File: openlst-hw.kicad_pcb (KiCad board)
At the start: 4 copper layers, 95.9 x 90.2 mm, 170 parts, among them J2 CC Prog/Debug, J3 UART0, J4 UART1, J5 Control Outputs, J6 ANT, J7 PC104-1, J8 PC104-2, U1 LM1117-3.3, U2 CC1110, U3 RFFM6406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

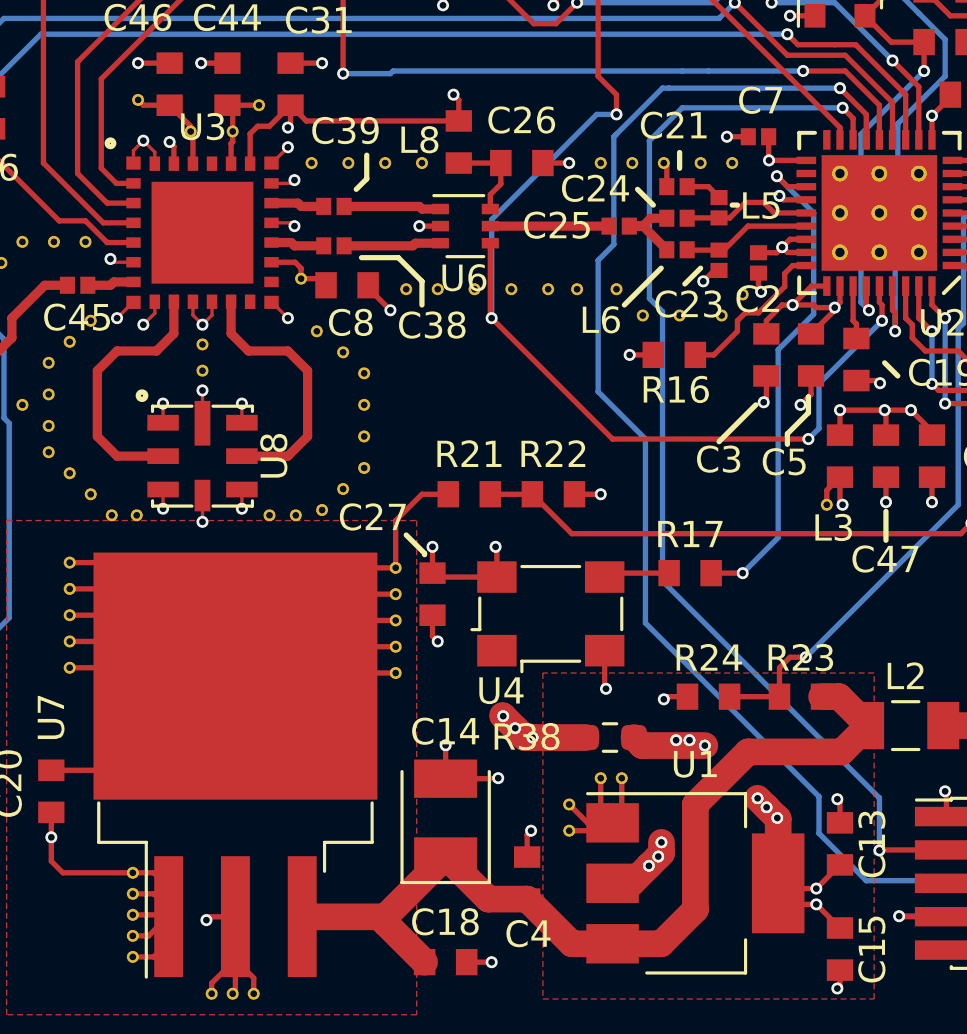
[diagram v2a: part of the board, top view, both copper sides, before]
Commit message: CAM: updated layout to fix some issues with ground plane arrangement
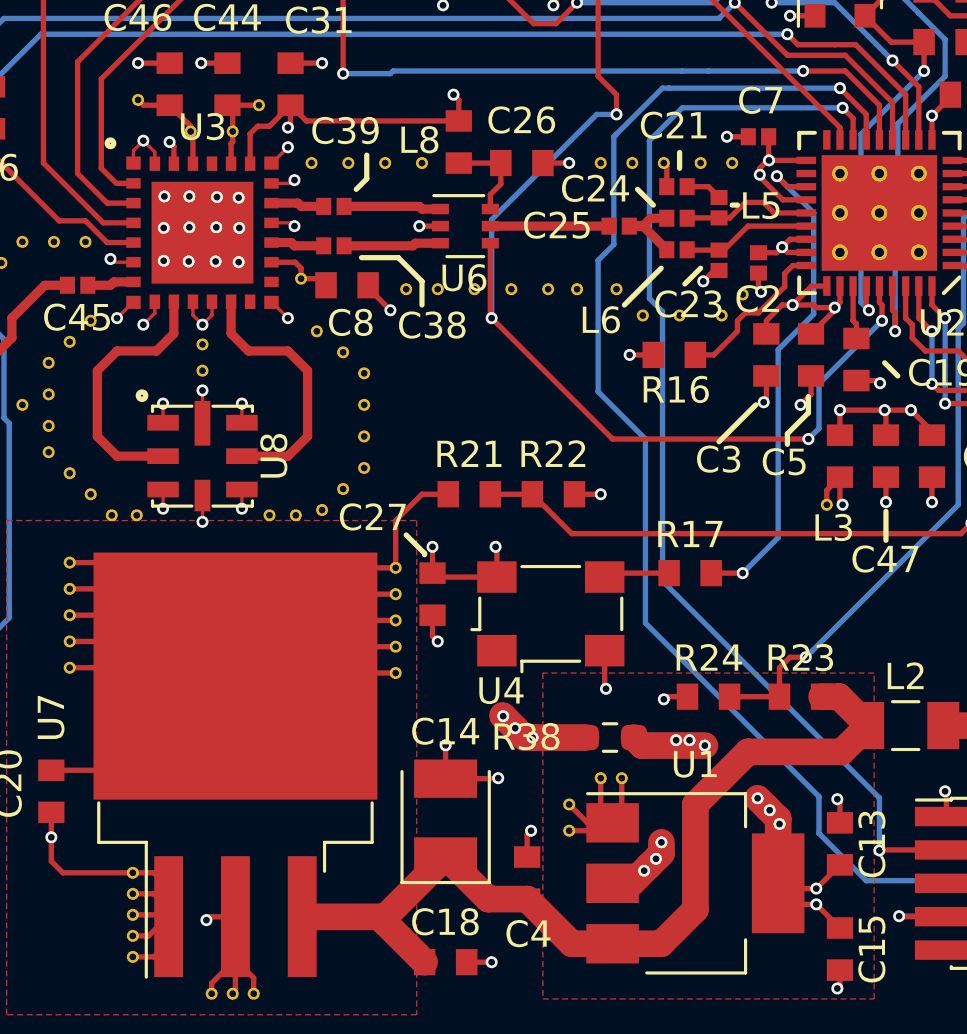
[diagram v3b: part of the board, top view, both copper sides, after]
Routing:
- net /3V3_FILT: track 24.4 -> 26.2 mm
- net GND: vias 59 -> 71
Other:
- board text removed: "This work is licensed under a Creative Commons Attribution-ShareAlike 4.0 International License (CC-BY-SA 4.0)."
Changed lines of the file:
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@@
     (effects (font (size 1 1) (thickness 0.15)) (justify mirror))
-  )
-  (gr_text "This work is licensed under a\nCreative Commons Attribution-ShareAlike 4.0\nInternational License (CC-BY-SA 4.0)." (at 69.5738 164.5054 180) (layer "B.SilkS")
-    (effects (font (size 1 1) (thickness 0.15)) (justify left mirror))
   )
   (gr_text "~{RX}" (at 87.6738 125.1054 180) (layer "F.SilkS")
@@
   (segment (start 104.5738 140.5054) (end 103.8738 140.5054) (width 0.2032) (layer "F.Cu") (net 1))
   (segment (start 102.0738 135.3054) (end 102.7738 134.6054) (width 0.2032) (layer "F.Cu") (net 1))
-  (segment (start 96.4238 138.5054) (end 96.2738 138.3554) (width 0.2032) (layer "F.Cu") (net 1))
   (segment (start 100.3238 146.5554) (end 100.2738 146.5054) (width 0.2032) (layer "F.Cu") (net 1))
   (segment (start 101.2738 146.5054) (end 102.0738 147.3054) (width 0.2032) (layer "F.Cu") (net 1))
   (segment (start 100.2738 146.5054) (end 98.5738 146.5054) (width 0.2032) (layer "F.Cu") (net 1))
   (segment (start 100.3238 147.4554) (end 100.3238 146.5554) (width 0.2032) (layer "F.Cu") (net 1))
+  (segment (start 95.525 137.55) (end 95.525 137.633443) (width 0.2032) (layer "F.Cu") (net 1))
   (segment (start 98.3738 142.6054) (end 98.3738 142.7054) (width 0.2032) (layer "F.Cu") (net 1))
   (segment (start 102.7738 134.5054) (end 102.7738 134.6054) (width 0.2032) (layer "F.Cu") (net 1))
@@
   (segment (start 104.8238 140.7554) (end 104.8238 141.4554) (width 0.2032) (layer "F.Cu") (net 1))
   (segment (start 98.5738 141.7854) (end 98.5738 142.4054) (width 0.2032) (layer "F.Cu") (net 1))
+  (segment (start 95.525 137.55) (end 95.525 137.3) (width 0.2032) (layer "F.Cu") (net 1))
   (segment (start 97.4938 141.7854) (end 98.0738 141.7854) (width 0.2032) (layer "F.Cu") (net 1))
+  (segment (start 96.396957 138.5054) (end 97.2938 138.5054) (width 0.2032) (layer "F.Cu") (net 1))
   (segment (start 95.8613 136.1054) (end 95.8613 136.9929) (width 0.2032) (layer "F.Cu") (net 1))
   (segment (start 98.3738 142.6054) (end 97.6738 142.6054) (width 0.2032) (layer "F.Cu") (net 1))
@@
   (segment (start 95.4738 140.5179) (end 96.1613 140.5179) (width 0.2032) (layer "F.Cu") (net 1))
   (segment (start 95.8738 137.0054) (end 97.2938 137.0054) (width 0.2032) (layer "F.Cu") (net 1))
+  (segment (start 95.525 137.3) (end 95.8196 137.0054) (width 0.2032) (layer "F.Cu") (net 1))
+  (segment (start 95.525 137.633443) (end 96.396957 138.5054) (width 0.2032) (layer "F.Cu") (net 1))
   (segment (start 102.0738 136.2254) (end 102.0738 135.3054) (width 0.2032) (layer "F.Cu") (net 1))
+  (segment (start 95.8196 137.0054) (end 95.8738 137.0054) (width 0.2032) (layer "F.Cu") (net 1))
   (segment (start 102.0738 147.4554) (end 102.0738 147.3054) (width 0.2032) (layer "F.Cu") (net 1))
   (segment (start 102.8538 140.5054) (end 103.8738 140.5054) (width 0.2032) (layer "F.Cu") (net 1))
   (segment (start 95.7738 143.6054) (end 95.7738 143.1054) (width 0.2032) (layer "F.Cu") (net 1))
   (segment (start 98.5738 147.4554) (end 98.5738 146.5054) (width 0.2032) (layer "F.Cu") (net 1))
-  (segment (start 97.2938 138.5054) (end 96.4238 138.5054) (width 0.2032) (layer "F.Cu") (net 1))
   (via (at 102.0738 135.3054) (size 0.4572) (drill 0.254) (layers "F.Cu" "B.Cu") (net 1))
+  (via (at 95.525 137.55) (size 0.4572) (drill 0.254) (layers "F.Cu" "B.Cu") (net 1))
   (via (at 96.7738 142.5054) (size 0.4572) (drill 0.254) (layers "F.Cu" "B.Cu") (net 1))
   (via (at 103.8738 140.5054) (size 0.4572) (drill 0.254) (layers "F.Cu" "B.Cu") (net 1))
@@
   (via (at 100.2738 146.5054) (size 0.4572) (drill 0.254) (layers "F.Cu" "B.Cu") (net 1))
   (via (at 101.2738 146.5054) (size 0.4572) (drill 0.254) (layers "F.Cu" "B.Cu") (net 1))
-  (via (at 96.2738 138.3554) (size 0.4572) (drill 0.254) (layers "F.Cu" "B.Cu") (net 1))
   (via (at 98.5738 146.5054) (size 0.4572) (drill 0.254) (layers "F.Cu" "B.Cu") (net 1))
   (segment (start 76.9738 142.4054) (end 77.5738 143.0054) (width 0.127) (layer "F.Cu") (net 2))
@@
   (via (at 102.5738 161.0054) (size 0.4572) (drill 0.254) (layers "F.Cu" "B.Cu") (net 2))
   (via (at 83.5738 159.2554) (size 0.4572) (drill 0.254) (layers "F.Cu" "B.Cu") (net 2))
+  (via (at 75.7 140.875) (size 0.4572) (drill 0.254) (layers "F.Cu" "B.Cu") (net 2))
   (via (at 77.5738 143.0054) (size 0.4572) (drill 0.254) (layers "F.Cu" "B.Cu") (net 2))
   (via (at 100.0988 145.4804) (size 0.4572) (drill 0.254) (layers "F.Cu" "B.Cu") (net 2))
@@
   (via (at 77.5738 136.5054) (size 0.4572) (drill 0.254) (layers "F.Cu" "B.Cu") (net 2))
   (via (at 55.6136 185.6038) (size 0.4572) (drill 0.254) (layers "F.Cu" "B.Cu") (net 2))
+  (via (at 73.825 139.55) (size 0.4572) (drill 0.254) (layers "F.Cu" "B.Cu") (net 2))
   (via (at 70.8238 140.7554) (size 0.4572) (drill 0.254) (layers "F.Cu" "B.Cu") (net 2))
   (via (at 95.6738 146.2054) (size 0.4572) (drill 0.254) (layers "F.Cu" "B.Cu") (net 2))
   (via (at 75.8238 146.2554) (size 0.4572) (drill 0.254) (layers "F.Cu" "B.Cu") (net 2))
+  (via (at 73.825 138.375) (size 0.4572) (drill 0.254) (layers "F.Cu" "B.Cu") (net 2))
   (via (at 64.2114 140.1254) (size 0.4572) (drill 0.254) (layers "F.Cu" "B.Cu") (net 2))
+  (via (at 74.875 138.4) (size 0.4572) (drill 0.254) (layers "F.Cu" "B.Cu") (net 2))
   (via (at 102.0738 150.0054) (size 0.4572) (drill 0.254) (layers "F.Cu" "B.Cu") (net 2))
+  (via (at 72.875 138.375) (size 0.4572) (drill 0.254) (layers "F.Cu" "B.Cu") (net 2))
   (via (at 85.3238 167.5054) (size 0.4572) (drill 0.254) (layers "F.Cu" "B.Cu") (net 2))
   (via (at 66.2738 133.1054) (size 0.4572) (drill 0.254) (layers "F.Cu" "B.Cu") (net 2))
@@
   (via (at 62.2738 133.1054) (size 0.4572) (drill 0.254) (layers "F.Cu" "B.Cu") (net 2))
   (via (at 89.4738 149.7054) (size 0.4572) (drill 0.254) (layers "F.Cu" "B.Cu") (net 2))
+  (via (at 75.7 138.425) (size 0.4572) (drill 0.254) (layers "F.Cu" "B.Cu") (net 2))
+  (via (at 75.725 139.575) (size 0.4572) (drill 0.254) (layers "F.Cu" "B.Cu") (net 2))
   (via (at 77.8238 137.7554) (size 0.4572) (drill 0.254) (layers "F.Cu" "B.Cu") (net 2))
   (via (at 74.3238 145.7554) (size 0.4572) (drill 0.254) (layers "F.Cu" "B.Cu") (net 2))
@@
   (via (at 96.6738 131.5054) (size 0.4572) (drill 0.254) (layers "F.Cu" "B.Cu") (net 2))
   (via (at 74.3238 150.7554) (size 0.4572) (drill 0.254) (layers "F.Cu" "B.Cu") (net 2))
+  (via (at 73.8 140.85) (size 0.4572) (drill 0.254) (layers "F.Cu" "B.Cu") (net 2))
   (via (at 77.8238 139.5054) (size 0.4572) (drill 0.254) (layers "F.Cu" "B.Cu") (net 2))
   (via (at 94.2738 136.1054) (size 0.4572) (drill 0.254) (layers "F.Cu" "B.Cu") (net 2))
@@
   (via (at 104.4738 132.5054) (size 0.4572) (drill 0.254) (layers "F.Cu" "B.Cu") (net 2))
   (via (at 85.5738 160.5054) (size 0.4572) (drill 0.254) (layers "F.Cu" "B.Cu") (net 2))
+  (via (at 74.825 140.85) (size 0.4572) (drill 0.254) (layers "F.Cu" "B.Cu") (net 2))
+  (via (at 72.85 139.575) (size 0.4572) (drill 0.254) (layers "F.Cu" "B.Cu") (net 2))
   (via (at 97.0738 146.3054) (size 0.4572) (drill 0.254) (layers "F.Cu" "B.Cu") (net 2))
   (via (at 68.5738 162.7554) (size 0.4572) (drill 0.254) (layers "F.Cu" "B.Cu") (net 2))
   (via (at 60.0966 140.1254) (size 0.4572) (drill 0.254) (layers "F.Cu" "B.Cu") (net 2))
+  (via (at 72.85 140.825) (size 0.4572) (drill 0.254) (layers "F.Cu" "B.Cu") (net 2))
   (via (at 98.4738 161.3054) (size 0.4572) (drill 0.254) (layers "F.Cu" "B.Cu") (net 2))
   (via (at 100.3238 150.0054) (size 0.4572) (drill 0.254) (layers "F.Cu" "B.Cu") (net 2))
+  (via (at 74.85 139.55) (size 0.4572) (drill 0.254) (layers "F.Cu" "B.Cu") (net 2))
   (via (at 88.2738 137.1054) (size 0.4572) (drill 0.254) (layers "F.Cu" "B.Cu") (net 2))
   (segment (start 104.8738 144.1054) (end 104.7738 144.1054) (width 0.2032) (layer "B.Cu") (net 2))
@@
   (via (at 93.434 159.2644) (size 0.4572) (drill 0.254) (layers "F.Cu" "B.Cu") (net 58))
   (via (at 92.3418 159.0612) (size 0.4572) (drill 0.254) (layers "F.Cu" "B.Cu") (net 58))
-  (via (at 91.6622 163.487) (size 0.4572) (drill 0.254) (layers "F.Cu" "B.Cu") (net 58))
+  (via (at 91.575 163.575) (size 0.4572) (drill 0.254) (layers "F.Cu" "B.Cu") (net 58))
   (via (at 91.783 162.9474) (size 0.4572) (drill 0.254) (layers "F.Cu" "B.Cu") (net 58))
   (via (at 92.8498 159.0612) (size 0.4572) (drill 0.254) (layers "F.Cu" "B.Cu") (net 58))
-  (via (at 95.7835 161.6139) (size 0.4572) (drill 0.254) (layers "F.Cu" "B.Cu") (net 58))
+  (via (at 95.9 161.725) (size 0.4572) (drill 0.254) (layers "F.Cu" "B.Cu") (net 58))
   (via (at 97.6738 165.3054) (size 0.4572) (drill 0.254) (layers "F.Cu" "B.Cu") (net 58))
   (via (at 95.4406 161.271) (size 0.4572) (drill 0.254) (layers "F.Cu" "B.Cu") (net 58))
-  (via (at 96.1899 162.0203) (size 0.4572) (drill 0.254) (layers "F.Cu" "B.Cu") (net 58))
-  (via (at 91.3066 163.8426) (size 0.4572) (drill 0.254) (layers "F.Cu" "B.Cu") (net 58))
+  (via (at 96.275 162.25) (size 0.4572) (drill 0.254) (layers "F.Cu" "B.Cu") (net 58))
+  (via (at 91.125 164.025) (size 0.4572) (drill 0.254) (layers "F.Cu" "B.Cu") (net 58))
   (segment (start 92.8498 159.0612) (end 92.3418 159.0612) (width 1.016) (layer "In2.Cu") (net 58))
   (segment (start 92.3418 162.8074) (end 92.3418 159.0612) (width 1.016) (layer "In2.Cu") (net 58))
